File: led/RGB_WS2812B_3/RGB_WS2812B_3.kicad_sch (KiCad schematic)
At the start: 3 parts

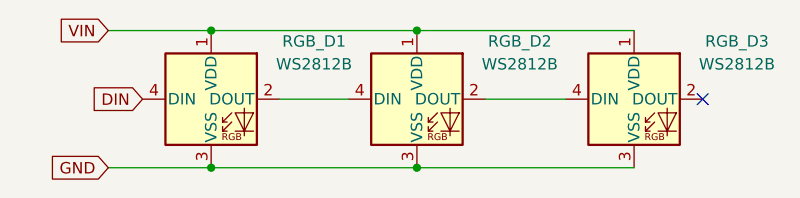
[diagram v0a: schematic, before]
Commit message: update RGB LEB pin name
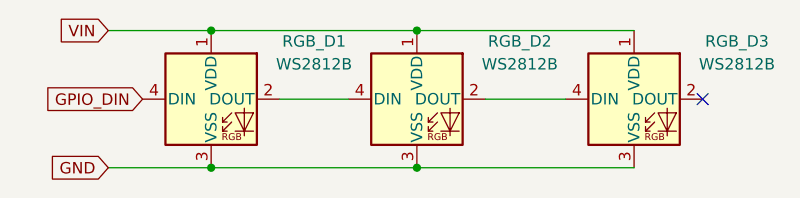
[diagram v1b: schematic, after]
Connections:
- net DIN renamed GPIO_DIN
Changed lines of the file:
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@@
 		)
 	)
-	(global_label "DIN"
+	(global_label "GPIO_DIN"
 		(shape input)
 		(at 105.41 71.12 180)
@@
 		)
 		(property "Intersheetrefs" "${INTERSHEET_REFS}"
-			(at 99.2195 71.12 0)
+			(at 93.7766 71.12 0)
 			(effects
 				(font

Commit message: use vcc instead of vin in led
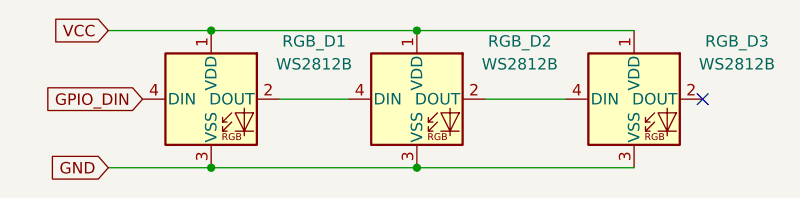
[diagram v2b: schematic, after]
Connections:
- net VIN renamed VCC
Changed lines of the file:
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@@
 		)
 	)
-	(global_label "VIN"
+	(global_label "VCC"
 		(shape input)
 		(at 101.6 63.5 180)
@@
 		)
 		(property "Intersheetrefs" "${INTERSHEET_REFS}"
-			(at 95.5909 63.5 0)
+			(at 94.9862 63.5 0)
 			(effects
 				(font

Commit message: update to 3.3V tag
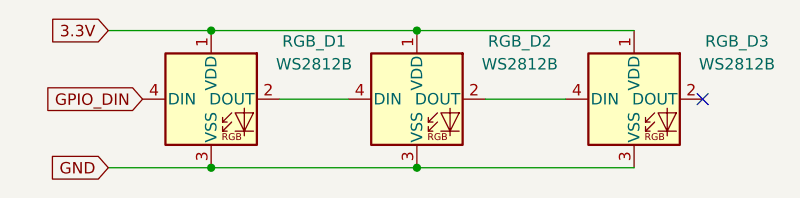
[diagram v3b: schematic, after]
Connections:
- net VCC renamed 3.3V
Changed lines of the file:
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@@
 		)
 	)
-	(global_label "VCC"
+	(global_label "3.3V"
 		(shape input)
 		(at 101.6 63.5 180)
@@
 		)
 		(property "Intersheetrefs" "${INTERSHEET_REFS}"
-			(at 94.9862 63.5 0)
+			(at 94.5024 63.5 0)
 			(effects
 				(font
